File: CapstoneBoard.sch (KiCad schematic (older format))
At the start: 42 parts, among them J1 Battery Conn, J10 Conn_02x02_Odd_Even, J2 IMU_COMM, J3 IMU_EXTRA, J4 SERVO_FEEDBACK, J5 Conn_FLIR, J6 Conn_LIDAR, J7 Conn_Servo_Driver, J8 Conn_01x04, J9 Jetson_Nano_Header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

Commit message: PCB Rev 3
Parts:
- removed J10: Conn_02x02_Odd_Even, Connector_PinHeader_2.54mm:PinHeader_2x02_P2.54mm_Vertical, symbol Connector_Generic:Conn_02x02_Odd_Even
- added C11: 100n, Capacitor_SMD:C_1206_3216Metric_Pad1.33x1.80mm_HandSolder, symbol Device:C
- added J11: Conn_01x04, Connector_PinHeader_2.54mm:PinHeader_1x06_P2.54mm_Vertical, symbol Connector_Generic:Conn_01x06
- added J12: Conn_01x02, Connector_PinHeader_2.54mm:PinHeader_1x02_P2.54mm_Vertical, symbol Connector_Generic:Conn_01x02
- added JP1: WP, Jumper:SolderJumper-2_P1.3mm_Open_Pad1.0x1.5mm, symbol Jumper:SolderJumper_2_Open
- added R1: 1k, Resistor_SMD:R_1206_3216Metric_Pad1.30x1.75mm_HandSolder, symbol Device:R
- added R12, R13: 3.9k, Resistor_SMD:R_1206_3216Metric_Pad1.30x1.75mm_HandSolder, symbol Device:R
- added U3: CAT24C32, Package_SO:TSSOP-8_4.4x3mm_P0.65mm, symbol capstoneParts:CAT24C32
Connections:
- net +3V3: now also C11.1, R1.1, R12.1, R13.1, U3.8 (VCC)
- net GND: now also C11.2, JP1.2 (B), U3.1 (A0), U3.2 (A1), U3.3 (A2), U3.4 (GND)
- net SCL1: now also J12.1 (Pin_1)
- net SDA1: now also J12.2 (Pin_2)
- net I2S_SCK: now reaches J9.12 (GPIO18/I2S0_SClK)
- net I2S_SCK: now also J11.4 (Pin_4)
- net GPIO6: now reaches J9.31 (CAM_MCLK/GPIO6)
- net GPIO6: now also J11.5 (Pin_5)
- net GPIO12: now reaches J9.32 (PWM0/GPIO12)
- net GPIO12: now also J11.6 (Pin_6)
- net I2S_FS: now reaches J9.35 (GPIO19/I2S0_FS)
- net I2S_FS: now also J11.3 (Pin_3)
- net I2S_DIN: now reaches J9.38 (GPIO20/I2S0_DIN)
- net I2S_DIN: now also J11.2 (Pin_2)
- net I2S_DOUT: now reaches J9.40 (GPIO21/I2S0_DOUT)
- net I2S_DOUT: now also J11.1 (Pin_1)
- net SCL2 renamed ID_SC
- net ID_SC: now also R12.2, U3.6 (SCL)
- net SDA2 renamed ID_SD
- net ID_SD: now also R13.2, U3.5 (SDA)
- new net WP: JP1.1 (A), R1.2, U3.7 (WP)
- no-connect marks 8 -> 3
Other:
- note added: "I2C Header"
- note added: "I2C/GPIO Header"
- note added: "Unclear if ID_EEPROM is used by Jetson. \nLeave this unpopulated untill we know for sure."

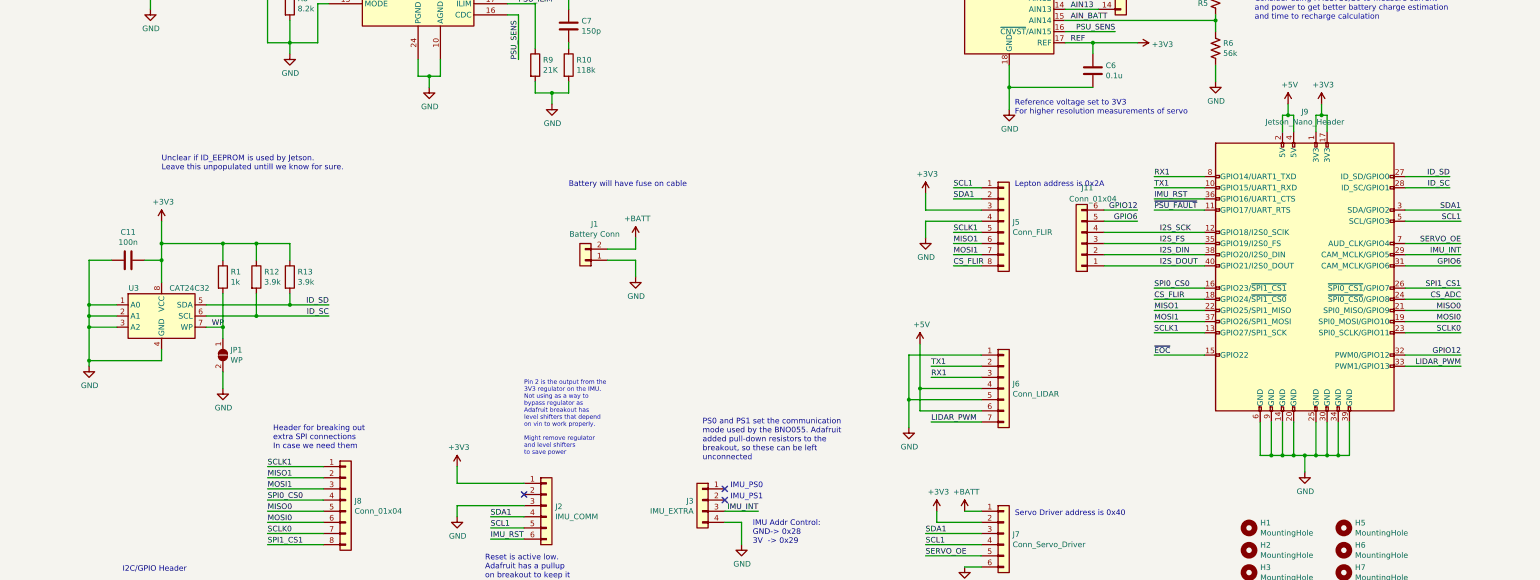
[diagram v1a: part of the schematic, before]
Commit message: Update board for better soldering without plated drills.
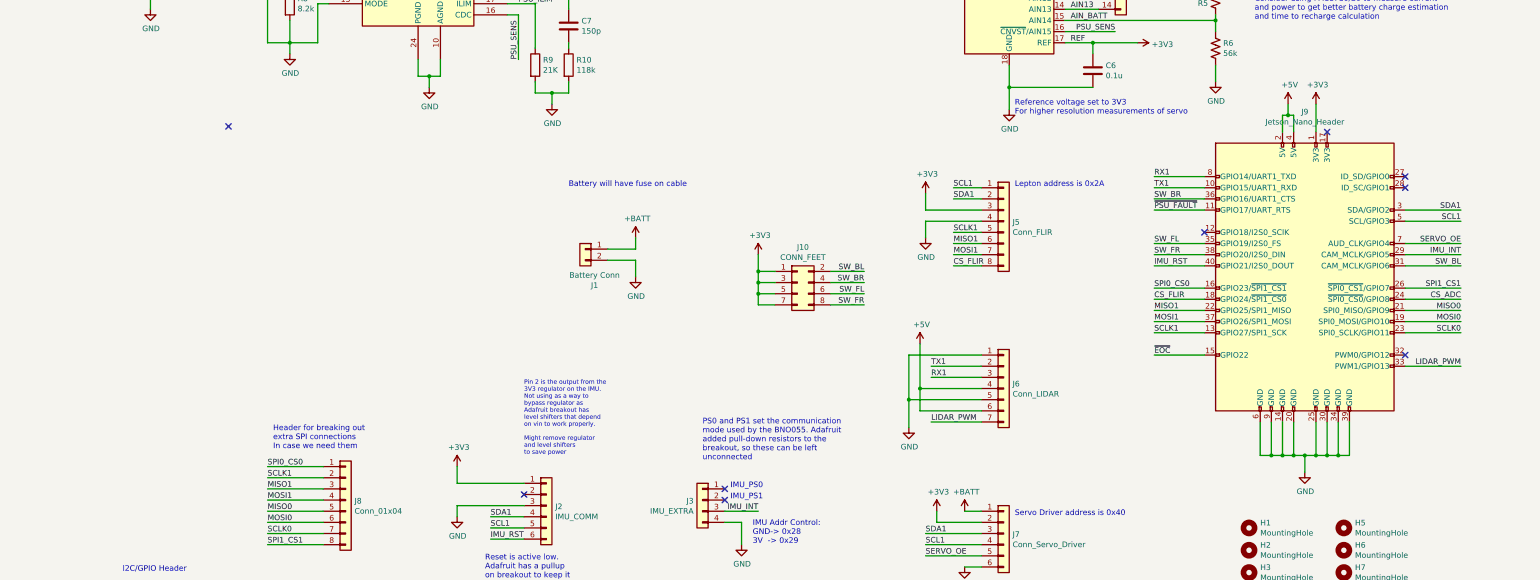
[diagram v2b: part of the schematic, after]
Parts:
- removed C11: 100n, Capacitor_SMD:C_1206_3216Metric_Pad1.33x1.80mm_HandSolder, symbol Device:C
- removed J11: Conn_01x04, Connector_PinHeader_2.54mm:PinHeader_1x06_P2.54mm_Vertical, symbol Connector_Generic:Conn_01x06
- removed JP1: WP, Jumper:SolderJumper-2_P1.3mm_Open_Pad1.0x1.5mm, symbol Jumper:SolderJumper_2_Open
- removed R1: 1k, Resistor_SMD:R_1206_3216Metric_Pad1.30x1.75mm_HandSolder, symbol Device:R
- removed R12, R13: 3.9k, Resistor_SMD:R_1206_3216Metric_Pad1.30x1.75mm_HandSolder, symbol Device:R
- removed U3: CAT24C32, Package_SO:TSSOP-8_4.4x3mm_P0.65mm, symbol capstoneParts:CAT24C32
- added J10: CONN_FEET, Connector_PinHeader_2.54mm:PinHeader_2x04_P2.54mm_Vertical, symbol Connector_Generic:Conn_02x04_Odd_Even
- J1: footprint Connector_AMASS:AMASS_XT60-M_1x02_P7.20mm_Vertical -> CapstoneParts:wireConn2
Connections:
- net I2S_DOUT is gone; now on net IMU_RST: J9.40 (GPIO21/I2S0_DOUT)
- net +3V3: now also J10.1 (Pin_1), J10.3 (Pin_3), J10.5 (Pin_5), J10.7 (Pin_7); no longer J9.17 (3V3)
- net +BATT: now also J1.1 (Pin_1); no longer J1.2 (Pin_2)
- net GND: now also J1.2 (Pin_2); no longer J1.1 (Pin_1)
- net IMU_RST: no longer J9.36 (GPIO16/UART1_CTS)
- net MISO1: now also J8.3 (Pin_3); no longer J8.2 (Pin_2)
- net MOSI1: now also J8.4 (Pin_4); no longer J8.3 (Pin_3)
- net SCLK1: now also J8.2 (Pin_2); no longer J8.1 (Pin_1)
- net SPI0_CS0: now also J8.1 (Pin_1); no longer J8.4 (Pin_4)
- net GPIO12: no longer names the net of J9.32 (PWM0/GPIO12)
- net GPIO6 renamed SW_BL
- net SW_BL: now also J10.2 (Pin_2)
- net I2S_DIN renamed SW_FR
- net SW_FR: now also J10.8 (Pin_8)
- net I2S_FS renamed SW_FL
- net SW_FL: now also J10.6 (Pin_6)
- net I2S_SCK: no longer names the net of J9.12 (GPIO18/I2S0_SClK)
- net ID_SC: no longer names the net of J9.28 (ID_SC/GPIO1)
- net ID_SD: no longer names the net of J9.27 (ID_SD/GPIO0)
- new net SW_BR: J10.4 (Pin_4), J9.36 (GPIO16/UART1_CTS)
- no-connect marks 3 -> 9
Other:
- note removed: "Unclear if ID_EEPROM is used by Jetson. \nLeave this unpopulated untill we know for sure."
